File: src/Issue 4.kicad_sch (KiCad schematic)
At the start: 199 parts, among them IC1 ULA, IC10 4116, IC11 4116, IC12 4116, IC13 4116, IC14 LM1889, IC15 4532, IC16 4532, IC17 4532, IC18 4532, IC19 4532, IC2 Z80, IC20 4532, IC21 4532, IC22 4532, IC23 74LS32, IC24 74LS00, IC25 74LS157, IC26 74LS157, IC3 LS157, IC4 LS157, IC5 ROM, IC6 4116, IC7 4116, IC8 4116, IC9 4116, J1 OKI, J10 UR3, J11 UR4, J2 TI, J3 TI, J4 TI, J7 Barrel_Jack_MountingPin, J8 UR1, J9 UR2, T1 Coil, X1 14Mhz, X2 4.43Mhz

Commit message: created ibom
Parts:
- C25, C27, C28, C29, C31, C32, C34, C35, C37, C38, C39, C41, C43, C44, C45, C46, C49, C50, C52, C53, C63, C64, C65, C67, C68, C69, C70, C71, C72, C73, C74, C75, C76, C79, C80, D1, D11, D13, D15, D17, D19, D2, D29, D3, D4, D5, D6, D7, D8, D9, E1, Ear0, IC1, IC10, IC11, IC12, IC13, IC14, IC15, IC16, IC17, IC18, IC19, IC2, IC20, IC21, IC22, IC23, IC24, IC25, IC26, IC3, IC4, IC5, IC6, IC7, IC8, IC9, J1, J10, J11, J2, J3, J4, J7, J8, J9, KB1, KB2, LS1, Mic0, R1, R10, R11, R12, R13, R14, R15, R16, R17, R18, R19, R2, R20, R21, R22, R23, R24, R25, R26, R27, R28, R29, R3, R30, R31, R32, R33, R34, R35, R36, R37, R4, R42, R43, R44, R45, R46, R47, R48, R49, R5, R50, R51, R52, R53, R56, R58, R59, R6, R60, R61, R62, R63, R64, R65, R66, R67, R68, R69, R7, R70, R71, R72, R73, R74, R75, R76, R77, R78, R79, R8, R9, REG1, T1, TR1, TR2, TR3, TR4, TR5, TR6, TR7, TR8, TR9, TV1, X1, X2: Fitted (none) -> 0; Sourced (none) -> 0
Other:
- company: Sinclair -> Submeson Brain Corporation

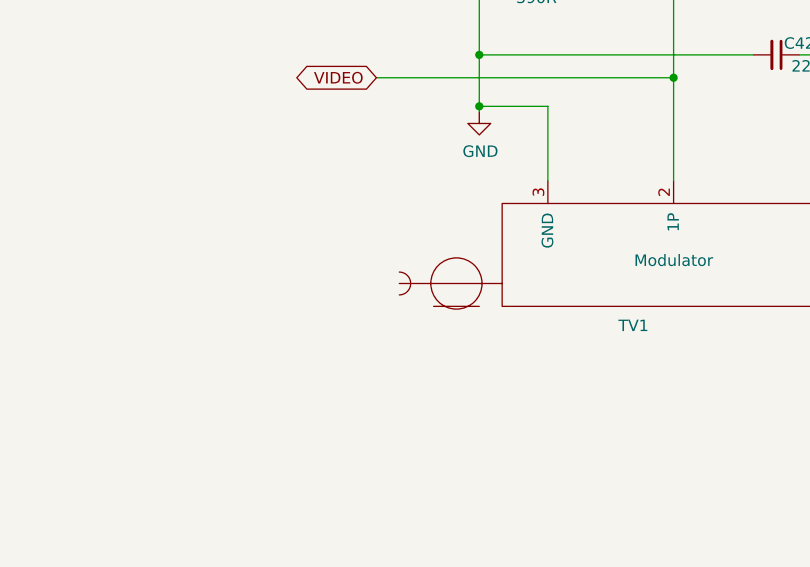
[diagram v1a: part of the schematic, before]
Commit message: re routed ear and mic and coil
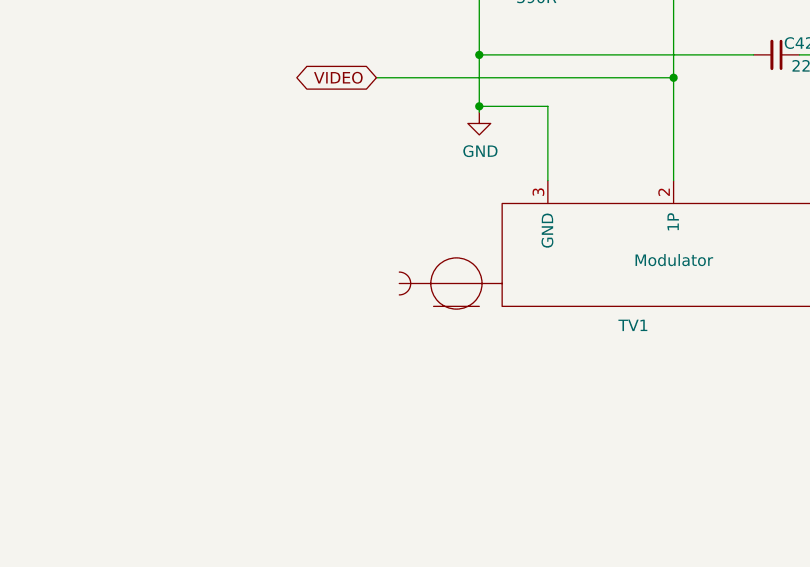
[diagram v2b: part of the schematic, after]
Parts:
- C25, C27, C28, C29, C31, C32, C34, C35, C37, C38, C39, C41, C43, C44, C45, C46, C49, C50, C52, C53, C63, C64, C65, C67, C68, C69, C70, C71, C72, C73, C74, C75, C76, C79, C80, D1, D11, D13, D15, D17, D19, D2, D29, D3, D4, D5, D6, D7, D8, D9, E1, Ear0, J1, J10, J11, J2, J3, J4, J7, J8, J9, KB1, KB2, LS1, Mic0, R1, R10, R11, R12, R13, R14, R15, R16, R17, R18, R19, R2, R20, R21, R22, R23, R24, R25, R26, R27, R28, R29, R3, R30, R31, R32, R33, R34, R35, R36, R37, R4, R42, R43, R44, R45, R46, R47, R48, R49, R5, R50, R51, R52, R53, R56, R58, R59, R6, R60, R61, R62, R63, R64, R65, R66, R67, R68, R69, R7, R70, R71, R72, R73, R74, R75, R76, R77, R78, R79, R8, R9, REG1, T1, TR1, TR2, TR3, TR4, TR5, TR6, TR7, TR8, TR9, TV1, X1, X2: Fitted 0 -> (none); Sourced 0 -> (none)
- IC1, IC2: footprint Package_DIP:DIP-40_W15.24mm -> Package_DIP:DIP-40_W15.24mm_Socket; Fitted 0 -> (none); Sourced 0 -> (none)
- IC10, IC11, IC12, IC13, IC15, IC16, IC17, IC18, IC19, IC20, IC21, IC22, IC25, IC26, IC3, IC4, IC6, IC7, IC8, IC9: footprint Package_DIP:DIP-16_W7.62mm -> Package_DIP:DIP-16_W7.62mm_Socket; Fitted 0 -> (none); Sourced 0 -> (none)
- IC14: footprint Package_DIP:DIP-18_W7.62mm -> Package_DIP:DIP-18_W7.62mm_Socket; Fitted 0 -> (none); Sourced 0 -> (none)
- IC23, IC24: footprint Package_DIP:DIP-14_W7.62mm -> Package_DIP:DIP-14_W7.62mm_Socket; Fitted 0 -> (none); Sourced 0 -> (none)
- IC23, IC24: footprint Package_DIP:DIP-14_W7.62mm -> (none); Fitted 0 -> (none); Sourced 0 -> (none)
- IC5: footprint Package_DIP:DIP-28_W15.24mm -> Package_DIP:DIP-28_W15.24mm_Socket; Fitted 0 -> (none); Sourced 0 -> (none)
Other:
- company: Submeson Brain Corporation -> Submeson Brain Corperation
- title: ZX Spectrum -> ZX Spectrum 48K
